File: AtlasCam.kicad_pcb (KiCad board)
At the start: 2 copper layers, 48.4 x 51.4 mm, 36 parts, among them J1 SD_Micro_TFPUSH, J2 USB_C_16Pin_C167321, U1 ESP32-S3-WROOM-1(N8R8), U2 LDO_3V3_2A_AIC1221-33GY3TR, U3 GR6206P282MR-G, U4 GR6206P182MR-G

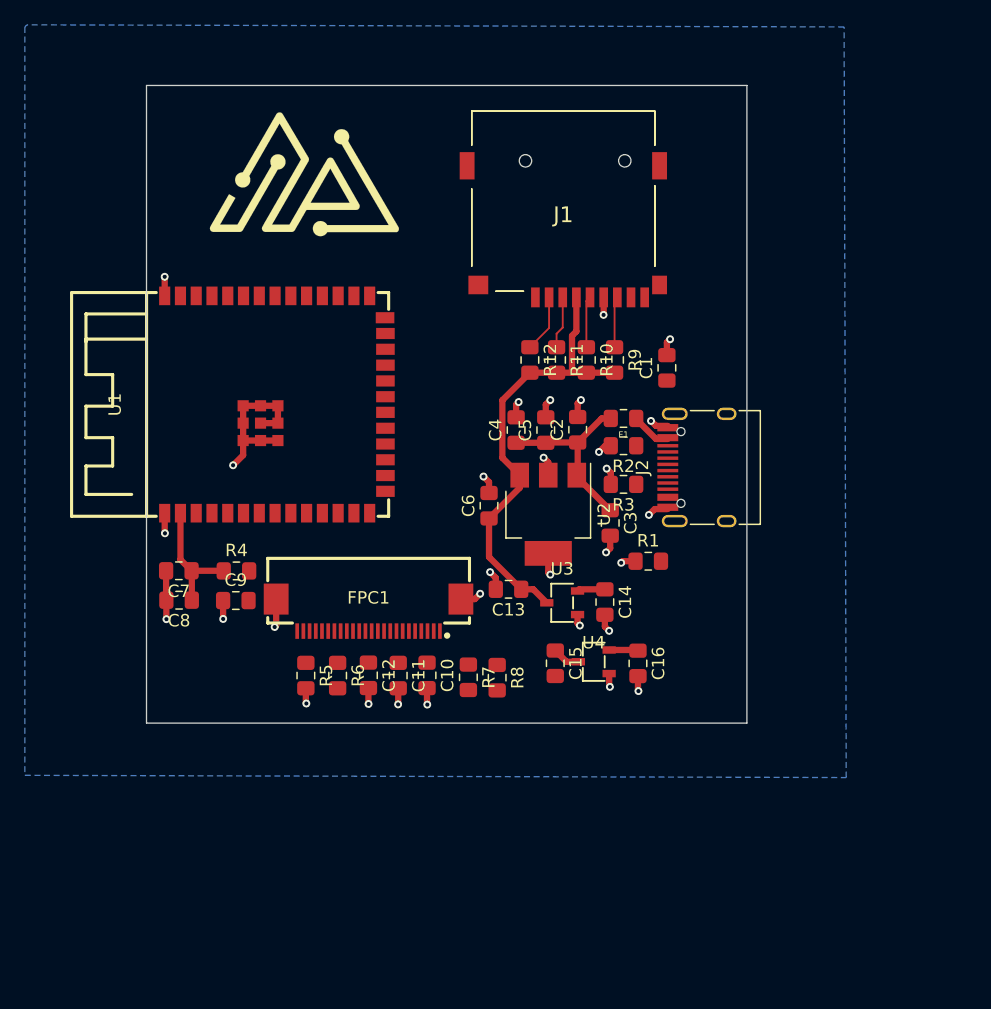
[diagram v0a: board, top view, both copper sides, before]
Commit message: First Draft: routiing, pulled D+/D- lines together, SD closer to edge
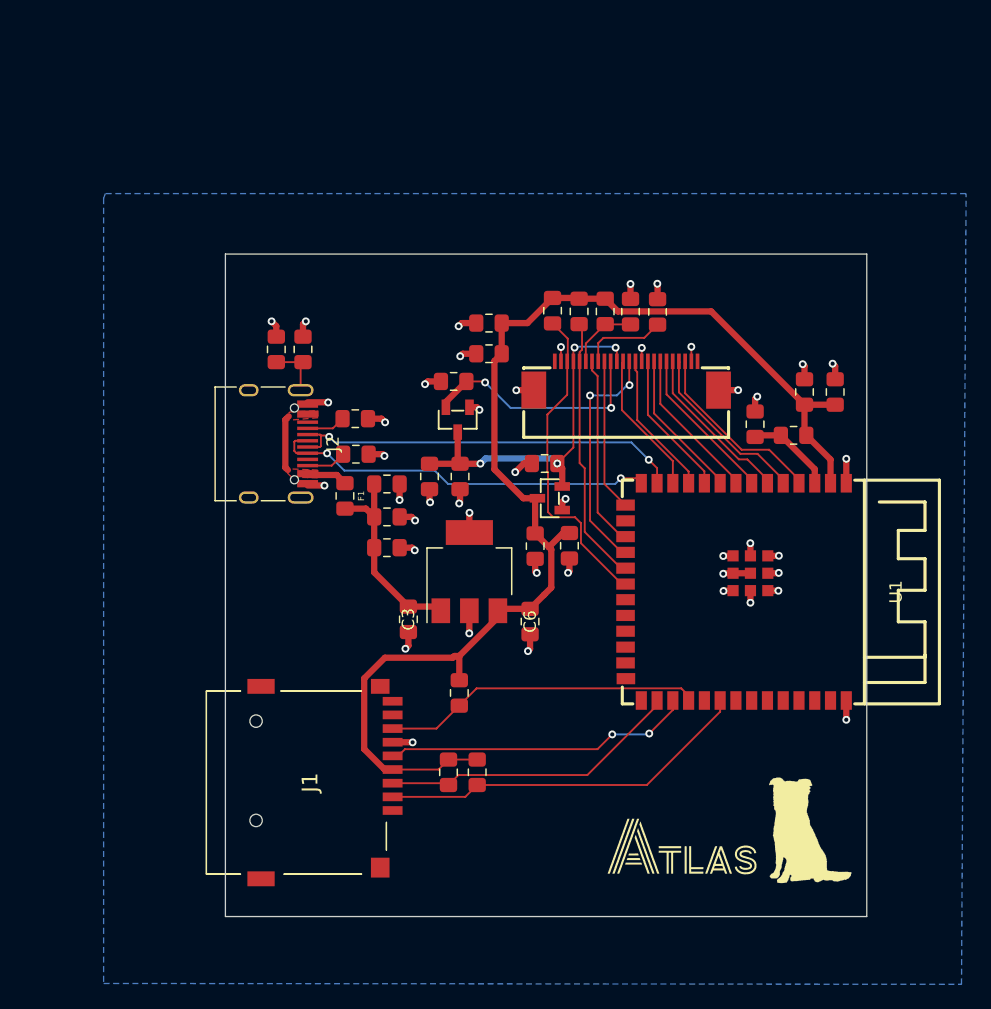
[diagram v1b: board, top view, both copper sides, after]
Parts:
- removed FPC1: FPC-05F-24PH20, easyeda2kicad:FPC-SMD_24P-P0.50_FPC-05F-24PH20
- removed R12: 4.7k, Remal_KiCadLib:R_0805_2012m
- removed U4: GR6206P182MR-G, easyeda2kicad:SOT-23-3_L2.9-W1.6-P1.90-LS2.8-BR
- added C17: 1uF, Remal_KiCadLib:C_0805_2012m, F.Cu at (154.5, 101.9)
- added C18: 1uF, Remal_KiCadLib:C_0805_2012m, F.Cu at (146.0, 96.2)
- added G***: LOGO, Remal_KiCadLib:Graphic_Atlas_v2_TextEN_12mm, F.Cu at (166.3, 126.0)
- added G***: LOGO, Remal_KiCadLib:Graphic_AtlasSil_v1_7mm, F.Cu at (176.7, 124.8)
- added Q1: JTD6206-28, easyeda2kicad:SOT-23-3_L2.9-W1.3-P1.90-LS2.4-BR, F.Cu at (155.7, 98.0)
- added Q2: JTD6206-12, easyeda2kicad:SOT-23-3_L2.9-W1.3-P1.90-LS2.4-BR, F.Cu at (148.3, 91.7)
- J2: footprint Remal_KiCadLib:USB_C_16Pin_C167321 -> Remal_KiCadLib:USB_C_16Pin_918-418K2023S40001
- R10, R11, R9: value 4.7k -> 10k
- U3: value GR6206P282MR-G -> 05A20L24P; footprint easyeda2kicad:SOT-23-3_L2.9-W1.6-P1.90-LS2.8-BR -> easyeda2kicad:FPC-SMD_24P-P0.50_05A20L24P
- moved C7 54.8 mm to (178.7, 89.4), turned to 90 degrees
- moved C8 53.1 mm to (176.2, 89.4), turned to 90 degrees
- moved J1 51.5 mm to (135.3, 120.9), turned to -90 degrees
- moved R4 46.2 mm to (175.3, 92.9), turned to 180 degrees
- moved C9 44.2 mm to (172.2, 92.0), turned to -90 degrees
- moved R5 40.7 mm to (164.4, 83.0), turned to 90 degrees
- moved U1 40.1 mm to (170.7, 105.5), turned to -90 degrees
- moved R6 36.4 mm to (160.1, 83.0), turned to 90 degrees
- moved J2 36.4 mm to (132.5, 93.6), turned to -90 degrees
- moved R10 35.0 mm to (147.5, 120.1), turned to 90 degrees
- moved R9 35.0 mm to (149.8, 120.1), turned to 90 degrees
- moved C10 33.6 mm to (162.2, 83.0), turned to 90 degrees
- moved R1 32.6 mm to (135.8, 86.0), turned to -90 degrees
- moved C1 31.5 mm to (133.7, 86.0)
- moved R7 30.8 mm to (158.0, 83.0), turned to 90 degrees
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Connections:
- C13 pad 1: 3V3_LDO -> 2V8_LDO
- C14 pad 1: 2V8_LDO -> 3V3_LDO
- C15 pad 1: 3V3_LDO -> 1V8_LDO
- C16 pad 1: 1V8_LDO -> 2V8_LDO
- R10 pad 1: SD_SCK -> SD_DI
- R11 pad 1: SD_DI -> SD_DO
- R5 pad 1: Net-(FPC1-Pad8) -> Net-(R5-Pad1)
- R9 pad 1: SD_DO -> SD_CS
- U1 pad 10: CAM_Y6 -> CAM_Y5
- U1 pad 11: CAM_Y7 -> CAM_Y6
- U1 pad 12: CAM_VSYNC -> CAM_Y7
- U1 pad 17: CAM_PCLK -> CAM_VSYNC
- U1 pad 19: CAM_SDA -> CAM_SCL
- U1 pad 20: CAM_SCL -> CAM_SDA
- U1 pad 21: SD_DO -> unconnected-(U1-IO13-Pad21)
- U1 pad 22: SD_SCK -> unconnected-(U1-IO14-Pad22)
- U1 pad 23: SD_CS -> unconnected-(U1-IO21-Pad23)
- U1 pad 28: unconnected-(U1-IO35-Pad28) -> SD_DI
- U1 pad 29: unconnected-(U1-IO36-Pad29) -> SD_SCK
- U1 pad 30: unconnected-(U1-IO37-Pad30) -> SD_DO
- U1 pad 32: unconnected-(U1-IO39-Pad32) -> SD_CS
- U1 pad 38: SD_DI -> unconnected-(U1-IO2-Pad38)
- U1 pad 4: CAM_Y0 -> CAM_Y2
- U1 pad 6: CAM_Y2 -> CAM_Y3
- U1 pad 7: CAM_Y3 -> CAM_Y0
- U1 pad 9: CAM_Y5 -> CAM_PCLK
- U3 pad 1: GND -> unconnected-(U3-Pad1)
- U3 pad 2: 2V8_LDO -> GND
- U3 pad 3: 3V3_LDO -> CAM_SDA
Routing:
- net 3V3_LDO: track 48.8 -> 101.2 mm
- net USB_D-: track 0.00 -> 32.4 mm, vias 0 -> 2
- net USB_D+: track 0.00 -> 31.6 mm, vias 0 -> 2
- net 2V8_LDO: track 2.26 -> 29.7 mm, vias 0 -> 4
- net CAM_SDA: track 0.00 -> 26.0 mm
- net SD_CS: track 4.65 -> 30.1 mm
- net SD_DO: track 4.11 -> 25.8 mm
- net CAM_SCL: track 0.00 -> 21.6 mm
- net SD_SCK: track 4.14 -> 24.9 mm, vias 0 -> 2
- net SD_DI: track 4.22 -> 24.4 mm
- net CAM_XCLK: track 0.00 -> 19.5 mm, vias 0 -> 2
- net 1V8_LDO: track 2.34 -> 19.1 mm, vias 0 -> 2
- net CAM_VSYNC: track 0.00 -> 15.4 mm
- net CAM_Y2: track 0.00 -> 15.3 mm
- net CAM_Y1: track 0.00 -> 14.6 mm
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- added copper zone on F.Cu, net Net-(F1-Pad1)
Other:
- board size 48.4 x 51.4 mm -> 51.7 x 53.4 mm

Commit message: Final Updates: pulled D-/D+ closer, moved SD Slot to edge, Verified design
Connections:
- net 1V8_LDO renamed 1V2_LDO
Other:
- board size 51.7 x 53.4 mm -> 51.7 x 52 mm
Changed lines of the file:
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@@
 	(net 6 "Net-(C10-Pad1)")
 	(net 7 "2V8_LDO")
-	(net 8 "1V8_LDO")
+	(net 8 "1V2_LDO")
 	(net 9 "Net-(F1-Pad1)")
 	(net 10 "CAM_Y3")
@@
 		(tags "capacitor handsolder")
 		(property "Reference" "C13"
-			(at 0 -1.65 360)
+			(at 0 -1.65 0)
 			(layer "F.SilkS")
 			(hide yes)
@@
 		)
 		(property "Value" "1uF"
-			(at 0 1.65 360)
+			(at 0 1.65 0)
 			(layer "F.Fab")
 			(effects
@@
 		)
 		(property "Footprint" "Remal_KiCadLib:C_0805_2012m"
-			(at 0 0 360)
+			(at 0 0 0)
 			(layer "F.Fab")
 			(hide yes)
@@
 		)
 		(property "Datasheet" ""
-			(at 0 0 360)
+			(at 0 0 0)
 			(layer "F.Fab")
 			(hide yes)
@@
 		)
 		(property "Description" "0805 (2012m) Capacitor"
-			(at 0 0 360)
+			(at 0 0 0)
 			(layer "F.Fab")
 			(hide yes)
@@
 		)
 		(fp_text user "${REFERENCE}"
-			(at 0 0 360)
+			(at 0 0 0)
 			(layer "F.Fab")
 			(effects
@@
 		(tags "capacitor handsolder")
 		(property "Reference" "C15"
-			(at 0 -1.65 360)
+			(at 0 -1.65 0)
 			(layer "F.SilkS")
 			(hide yes)
@@
 		)
 		(property "Value" "1uF"
-			(at 0 1.65 360)
+			(at 0 1.65 0)
 			(layer "F.Fab")
 			(effects
@@
 		)
 		(property "Footprint" "Remal_KiCadLib:C_0805_2012m"
-			(at 0 0 360)
+			(at 0 0 0)
 			(layer "F.Fab")
 			(hide yes)
@@
 		)
 		(property "Datasheet" ""
-			(at 0 0 360)
+			(at 0 0 0)
 			(layer "F.Fab")
 			(hide yes)
@@
 		)
 		(property "Description" "0805 (2012m) Capacitor"
-			(at 0 0 360)
+			(at 0 0 0)
 			(layer "F.Fab")
 			(hide yes)
@@
 		)
 		(fp_text user "${REFERENCE}"
-			(at 0 0 360)
+			(at 0 0 0)
 			(layer "F.Fab")
 			(effects
@@
 			(layers "F.Cu" "F.Paste" "F.Mask")
 			(roundrect_rratio 0.217391)
-			(net 8 "1V8_LDO")
+			(net 8 "1V2_LDO")
 			(pintype "passive")
 		)
@@
 			(size 0.3 1.25)
 			(layers "F.Cu" "F.Paste" "F.Mask")
-			(net 8 "1V8_LDO")
+			(net 8 "1V2_LDO")
 			(pinfunction "10")
 			(pintype "unspecified")
@@
 		(at 155.68 98)
 		(property "Reference" "Q1"
-			(at 0 0 360)
+			(at 0 0 0)
 			(layer "F.SilkS")
 			(hide yes)
@@
 		)
 		(property "Value" "JTD6206-28"
-			(at 3.32 3.49 360)
+			(at 3.32 3.49 0)
 			(layer "F.Fab")
 			(hide yes)
@@
 		)
 		(property "Footprint" "easyeda2kicad:SOT-23-3_L2.9-W1.3-P1.90-LS2.4-BR"
-			(at 0 0 360)
+			(at 0 0 0)
 			(layer "F.Fab")
 			(hide yes)
@@
 		)
 		(property "Datasheet" ""
-			(at 0 0 360)
+			(at 0 0 0)
 			(layer "F.Fab")
 			(hide yes)
@@
 		)
 		(property "Description" ""
-			(at 0 0 360)
+			(at 0 0 0)
 			(layer "F.Fab")
 			(hide yes)
@@
 		)
 		(fp_text user "${REFERENCE}"
-			(at 0 0 360)
+			(at 0 0 0)
 			(layer "F.Fab")
 			(effects
@@
 			(size 1.25 0.7)
 			(layers "F.Cu" "F.Paste" "F.Mask")
-			(net 8 "1V8_LDO")
+			(net 8 "1V2_LDO")
 			(pinfunction "VOUT")
 			(pintype "unspecified")
@@
 		)
 	)
-	(gr_rect
-		(start 129.55 78.33)
-		(end 181.21 131.69)
+	(gr_arc
+		(start 132.05 131.69)
+		(mid 130.282233 130.957767)
+		(end 129.55 129.19)
 		(stroke
 			(width 0.05)
 			(type default)
 		)
-		(fill none)
 		(layer "Edge.Cuts")
 	)
-	(gr_rect
-		(start 129.55 78.33)
-		(end 181.21 131.69)
+	(gr_line
+		(start 129.55 129.19)
+		(end 129.55 82.14)
+		(stroke
+			(width 0.05)
+			(type default)
+		)
+		(layer "Edge.Cuts")
+	)
+	(gr_line
+		(start 132.05 79.64)
+		(end 178.71 79.64)
+		(stroke
+			(width 0.05)
+			(type default)
+		)
+		(layer "Edge.Cuts")
+	)
+	(gr_arc
+		(start 129.55 82.14)
+		(mid 130.282233 80.372233)
+		(end 132.05 79.64)
+		(stroke
+			(width 0.05)
+			(type default)
+		)
+		(layer "Edge.Cuts")
+	)
+	(gr_line
+		(start 178.71 131.69)
+		(end 132.05 131.69)
+		(stroke
+			(width 0.05)
+			(type default)
+		)
+		(layer "Edge.Cuts")
+	)
+	(gr_arc
+		(start 178.71 79.64)
+		(mid 180.477767 80.372233)
+		(end 181.21 82.14)
+		(stroke
+			(width 0.05)
+			(type default)
+		)
+		(layer "Edge.Cuts")
+	)
+	(gr_line
+		(start 181.21 82.14)
+		(end 181.21 129.19)
+		(stroke
+			(width 0.05)
+			(type default)
+		)
+		(layer "Edge.Cuts")
+	)
+	(gr_arc
+		(start 181.21 129.19)
+		(mid 180.477767 130.957767)
+		(end 178.71 131.69)
+		(stroke
+			(width 0.05)
+			(type default)
+		)
+		(layer "Edge.Cuts")
+	)
+	(gr_arc
+		(start 132.05 131.69)
+		(mid 130.282233 130.957767)
+		(end 129.55 129.19)
+		(stroke
+			(width 0.5)
+			(type default)
+		)
+		(layer "Margin")
+	)
+	(gr_line
+		(start 129.55 129.19)
+		(end 129.55 82.14)
+		(stroke
+			(width 0.5)
+			(type default)
+		)
+		(layer "Margin")
+	)
+	(gr_line
+		(start 178.71 131.69)
+		(end 132.05 131.69)
+		(stroke
+			(width 0.5)
+			(type default)
+		)
+		(layer "Margin")
+	)
+	(gr_arc
+		(start 181.21 129.19)
+		(mid 180.477767 130.957767)
+		(end 178.71 131.69)
+		(stroke
+			(width 0.5)
+			(type default)
+		)
+		(layer "Margin")
+	)
+	(gr_arc
+		(start 129.55 82.14)
+		(mid 130.282233 80.372233)
+		(end 132.05 79.64)
+		(stroke
+			(width 0.5)
+			(type default)
+		)
+		(layer "Margin")
+	)
+	(gr_arc
+		(start 178.71 79.64)
+		(mid 180.477767 80.372233)
+		(end 181.21 82.14)
+		(stroke
+			(width 0.5)
+			(type default)
+		)
+		(layer "Margin")
+	)
+	(gr_line
+		(start 132.05 79.64)
+		(end 178.71 79.64)
+		(stroke
+			(width 0.5)
+			(type default)
+		)
+		(layer "Margin")
+	)
+	(gr_line
+		(start 181.21 82.14)
+		(end 181.21 129.19)
 		(stroke
 			(width 0.5)
 			(type default)
 		)
-		(fill none)
 		(layer "Margin")
 	)
